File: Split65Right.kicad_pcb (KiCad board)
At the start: 2 copper layers, 219.2 x 97.8 mm, 98 parts, among them J1 Jack4, J2 OLED, SW1 SW_PUSH, SW10 SW_PUSH, SW11 SW_PUSH, SW12 SW_PUSH, SW13 SW_PUSH, SW14 SW_PUSH, SW15 SW_PUSH, SW16 SW_PUSH, SW17 SW_PUSH, SW18 SW_PUSH, SW19 SW_PUSH, SW2 SW_PUSH, SW20 SW_PUSH, SW21 SW_PUSH, SW22 SW_PUSH, SW23 SW_PUSH, SW24 SW_PUSH, SW25 SW_PUSH, SW26 SW_PUSH, SW27 SW_PUSH, SW28 SW_PUSH, SW29 SW_PUSH, SW3 SW_PUSH, SW30 SW_PUSH, SW31 SW_PUSH, SW32 SW_PUSH, SW33 SW_PUSH, SW34 SW_PUSH, SW35 SW_PUSH, SW36 SW_PUSH, SW37 SW_PUSH, SW38 SW_PUSH, SW39 SW_PUSH, SW4 SW_PUSH, SW40 SW_PUSH, SW5 SW_PUSH, SW6 SW_PUSH, SW7 SW_PUSH, SW8 SW_PUSH, SW9 SW_PUSH, U1 proton_c

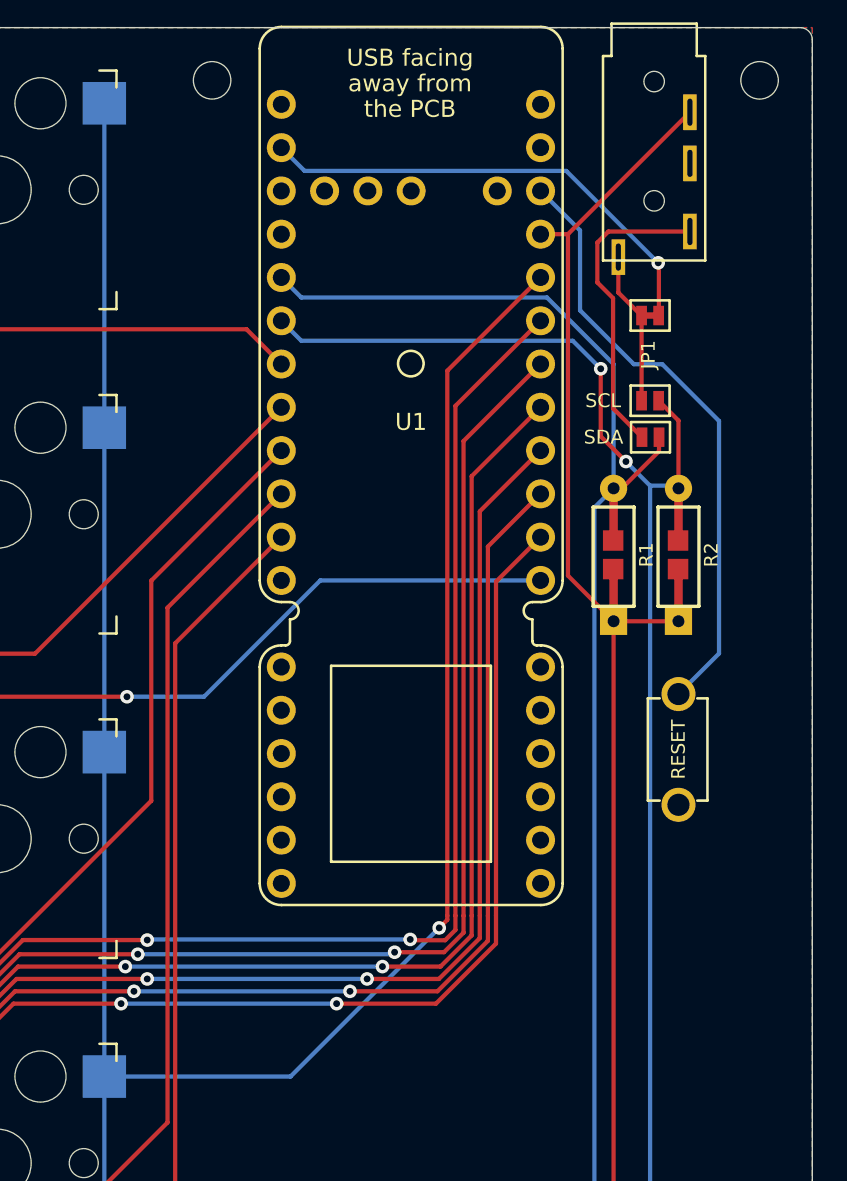
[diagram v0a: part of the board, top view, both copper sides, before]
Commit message: modified:   Split65Left-cache.lib 	modified:   Split65Left.kicad_pcb 	modified:   Split65Left.kicad_pcb-bak 	modified:   Split65Left.net 	modified:   Split65Left.sch 	modified:   Split65Left.sch-bak 	modified:   Split65Right-cache.lib 	modified:   Split65Right.kicad_pcb 	modified:   Split65Right.kicad_pcb-bak 	modified:   Split65Right.net 	modified:   Split65Right.sch 	modified:   Split65Right.sch-bak
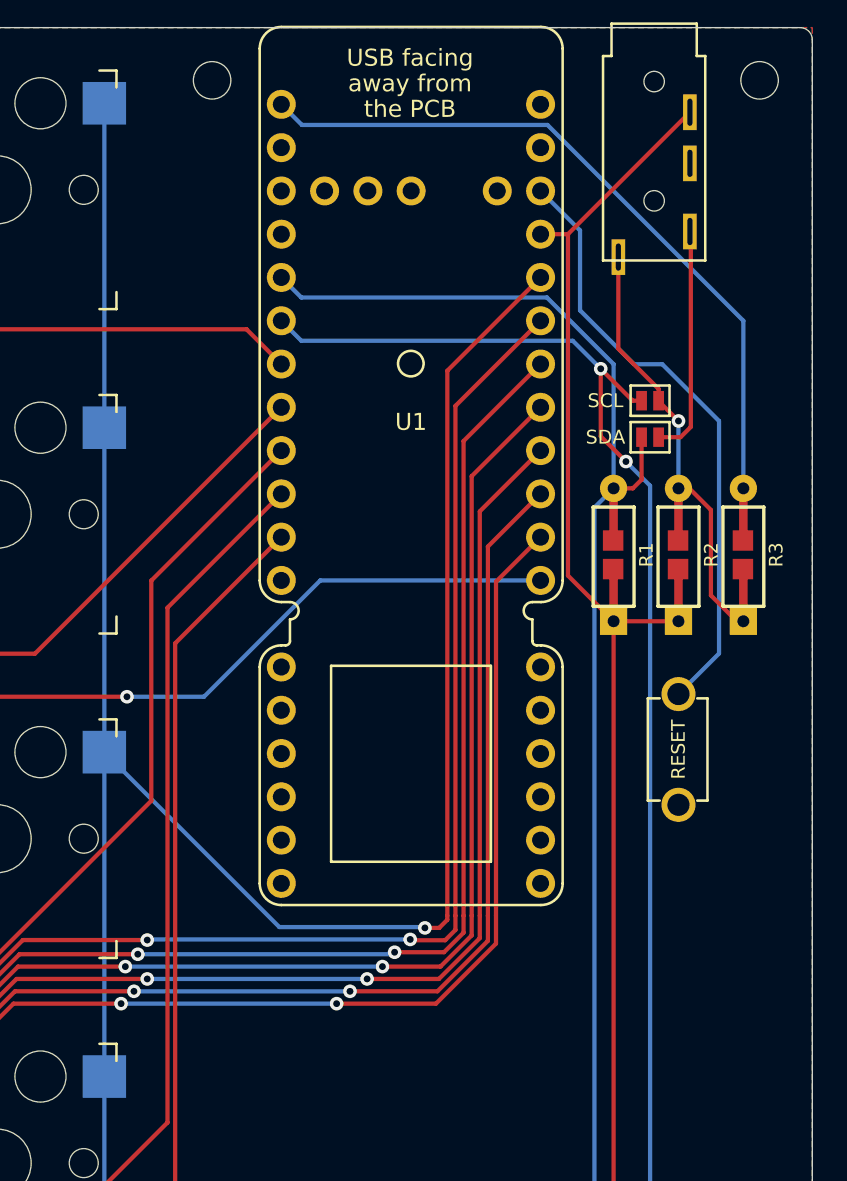
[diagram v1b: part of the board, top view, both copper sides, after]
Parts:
- removed JP1: Jumper, footprints:jumper_data
- added R3: 120, footprints:R_1608_axial, F.Cu at (236.6, 61.4)
- R1, R2: value R -> 5k
- turned JP2 to 180 degrees
- turned JP3 to 180 degrees
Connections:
- R2 pad 2: SCL -> Net-(J1-PadT)
- U1 pad A10: DATA -> Net-(U1-PadA10)
- U1 pad A9: LED -> DATA
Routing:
- net Net-(J1-PadT): track 8.99 -> 31.9 mm, vias 0 -> 1
- net DATA: track 28.0 -> 45.3 mm, vias 1 -> 0
- net SCL: track 110.0 -> 102.7 mm
- net Net-(J1-PadS): track 18.2 -> 13.6 mm
- net COL0: track 140.1 -> 140.7 mm

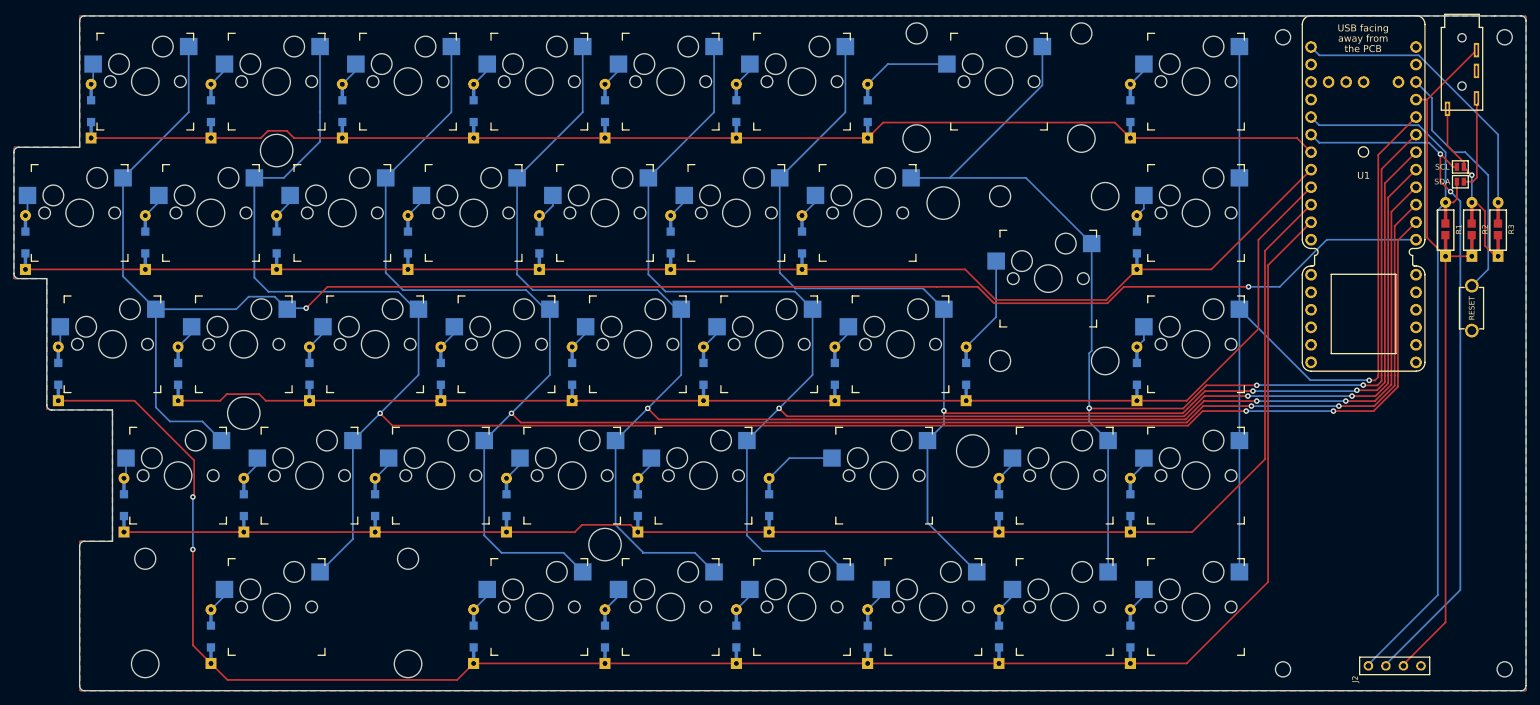
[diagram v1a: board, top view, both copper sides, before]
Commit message: Updated some small things - removed 3u buttons
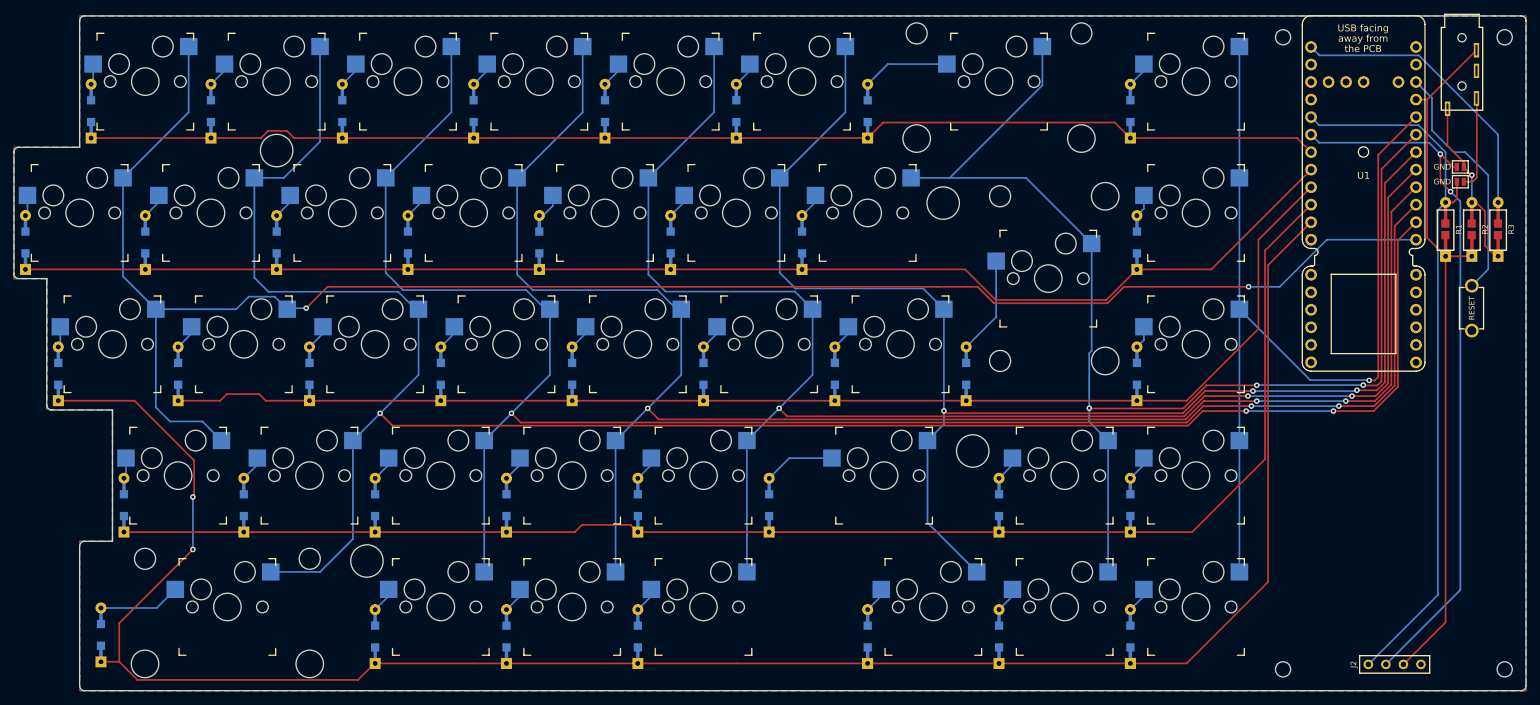
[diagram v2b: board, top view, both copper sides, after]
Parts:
- removed the HOLE_3M at (107.1, 107.1)
- JP2: value SDA -> GND
- JP3: value SCL -> GND
- SW39: footprint footprints:KailhSocket-3U -> footprints:KailhSocket-2.25U
- U1: value proton_c -> Proton_C
- moved HOLE_3M 27.9 mm to (72.6, 109.5)
- moved D39 15.9 mm to (34.0, 120.2)
- moved D36 14.3 mm to (111.9, 120.4)
- moved D37 14.3 mm to (92.8, 120.4)
- moved D38 14.3 mm to (73.8, 120.4)
- moved SW36 14.3 mm to (121.4, 116.1)
- moved SW37 14.3 mm to (102.3, 116.1)
- moved SW38 14.3 mm to (83.3, 116.1)
- moved SW39 7.14 mm to (52.4, 116.1)
- moved J2 3.82 mm to (217.8, 124.5)
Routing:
- net ROW4: track 268.7 -> 287.9 mm
- net COL5: track 274.2 -> 263.1 mm
- net COL3: track 239.5 -> 228.3 mm
- net COL4: track 255.9 -> 245.5 mm
- net Net-(D39-Pad2): track 3.74 -> 11.9 mm
- net COL6: track 285.2 -> 292.3 mm
